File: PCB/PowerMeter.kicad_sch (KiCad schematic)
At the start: 20 parts, among them J1 Conn_02x03_Top_Bottom, J2 Conn_01x06_Pin, J3 USB_B_Micro, SW1 SW_Push, U1 MCP1700x-330xxMB, U2 ESP32-C6-WROOM-1

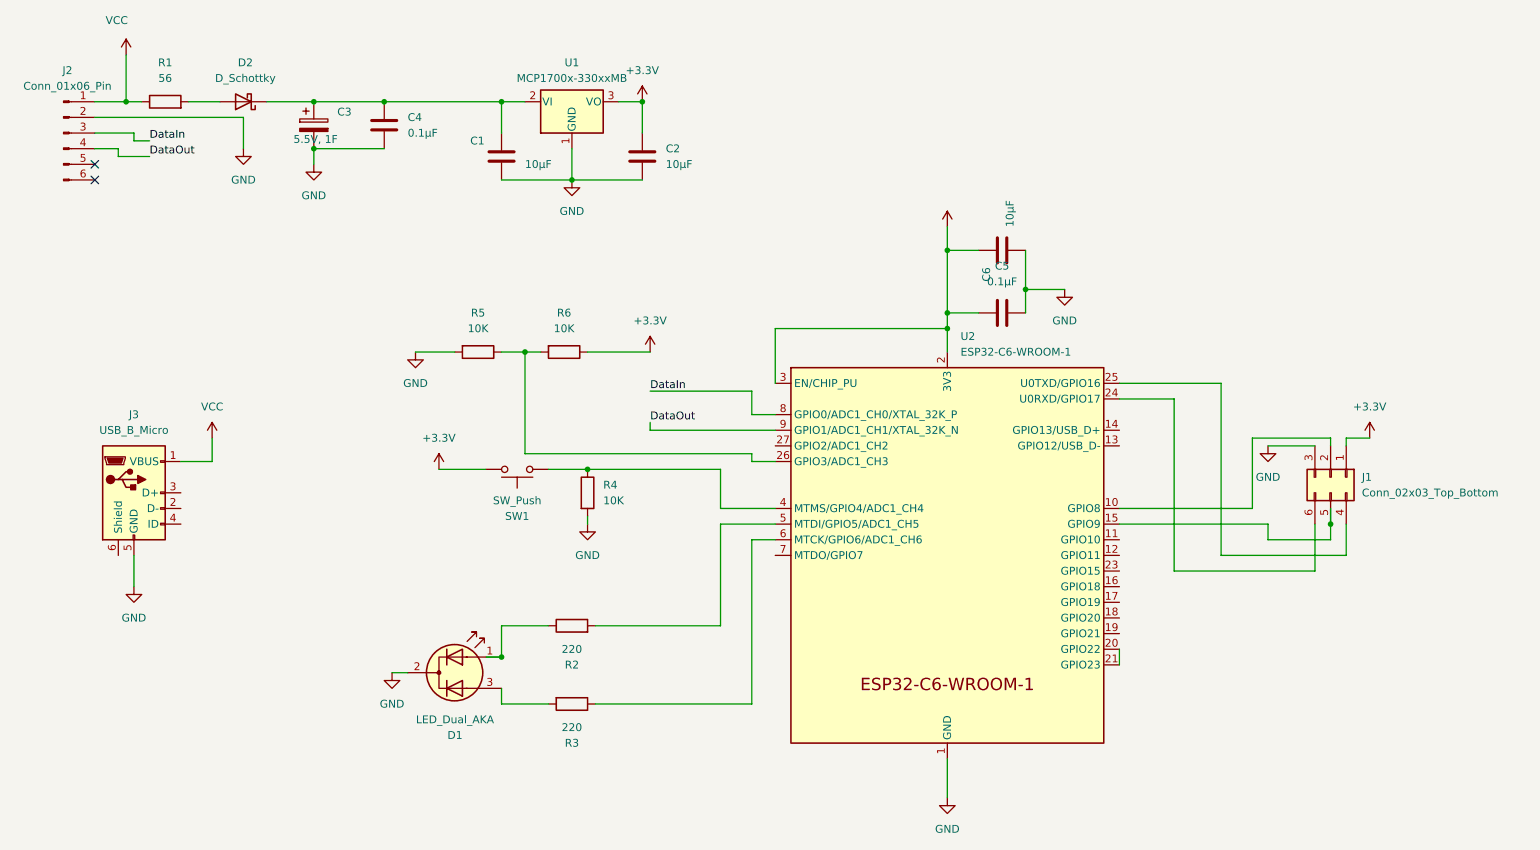
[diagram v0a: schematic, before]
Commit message: Added voltage measurement for 4.1 volt
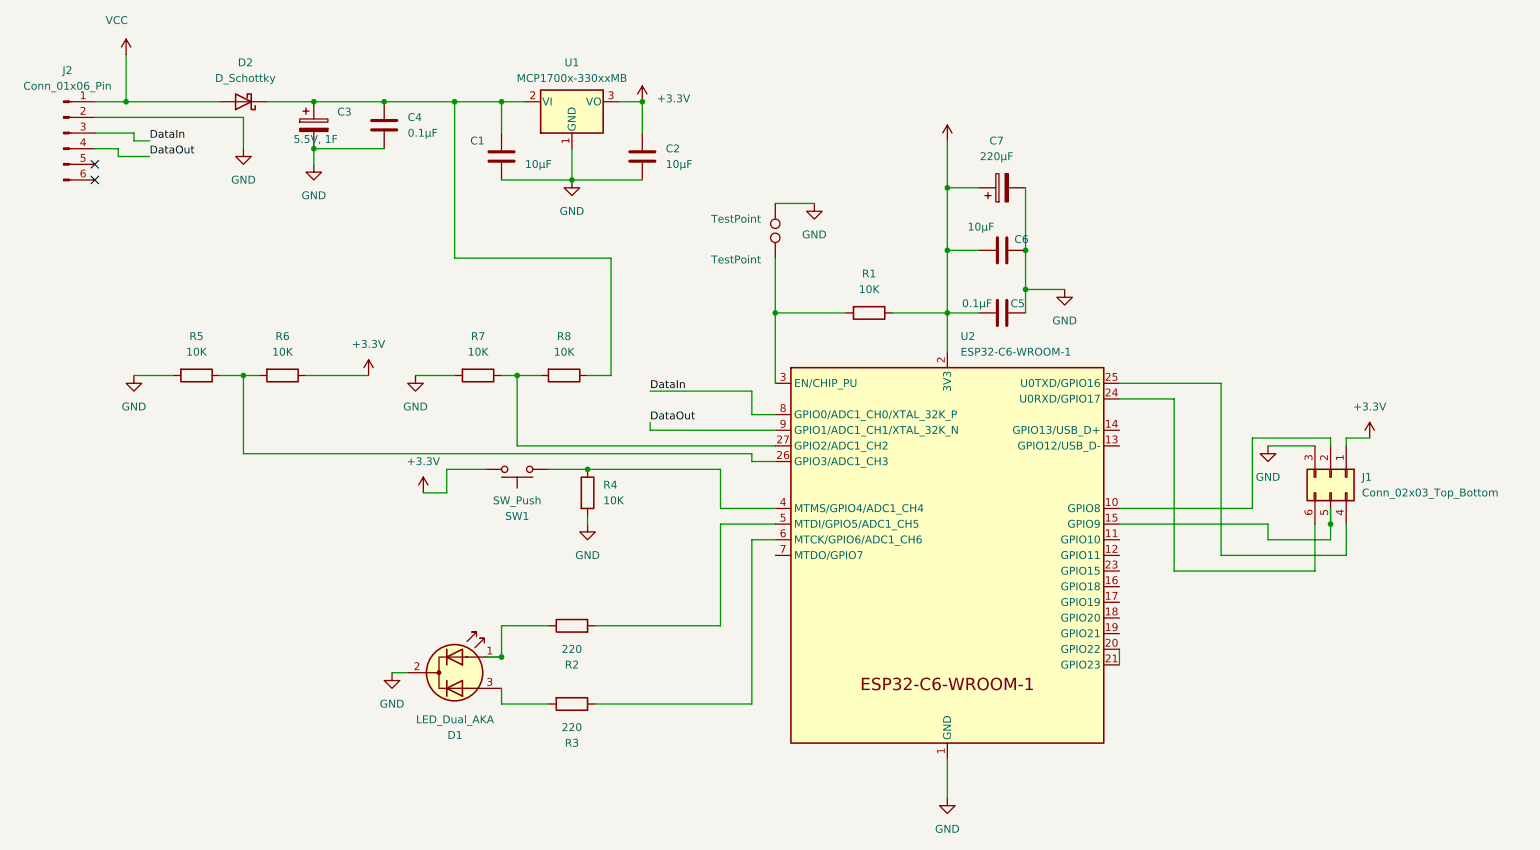
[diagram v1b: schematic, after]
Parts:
- removed J3: USB_B_Micro, Connector_USB:USB_Micro-B_Molex_47346-0001, symbol Connector:USB_B_Micro
- added C7: 220µF, Capacitor_SMD:C_1812_4532Metric, symbol Device:C_Polarized
- added R7, R8: 10K, Resistor_SMD:R_0805_2012Metric_Pad1.20x1.40mm_HandSolder, symbol Device:R
- added RST1, RST2: TestPoint, TestPoint:TestPoint_Pad_D2.0mm, symbol Connector:TestPoint
- C3: footprint Capacitor_THT:Peers Super -> Capacitor_THT:PHV-5R4H155-R
- R1: value 56 -> 10K
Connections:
- net +3.3V: now also R1.1, C7.1; no longer U2.3 (EN/CHIP_PU)
- net GND: now also C7.2, R7.2, RST1.1
- net VCC: now also D2.2 (A); no longer R1.1
- net at C1.1, C3.1, C4.1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: now also R8.1
- net at U2.27 (GPIO2/ADC1_CH2): now also R7.1, R8.2
- net at R1.2: now also U2.3 (EN/CHIP_PU), RST2.1; no longer D2.2 (A)
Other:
- title: (none) -> Wattzig
- moved on the sheet: R5, R6
